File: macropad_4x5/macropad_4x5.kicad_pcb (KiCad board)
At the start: 2 copper layers, 76.2 x 95.2 mm, 41 parts

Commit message: Updated schematic and pcb routing
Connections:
- B1 pad 17: col0 -> col2
- B1 pad 18: col1 -> col3
- B1 pad 19: col2 -> col1
- B1 pad 20: col3 -> col0
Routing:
- net row3: track 0.00 -> 140.5 mm
- net row4: track 0.00 -> 140.5 mm
- net col0: track 0.00 -> 131.3 mm
- net col3: track 0.00 -> 130.1 mm
- net row2: track 0.00 -> 122.9 mm
- net row0: track 0.00 -> 98.4 mm
- net col1: track 0.00 -> 96.6 mm
- net row1: track 0.00 -> 91.9 mm
- net col2: track 0.00 -> 88.6 mm
- net Net-(D4-Pad2): track 0.00 -> 23.3 mm
- net Net-(D8-Pad2): track 0.00 -> 23.3 mm
- net Net-(D16-Pad2): track 0.00 -> 23.3 mm
- net Net-(D5-Pad2): track 0.00 -> 23.3 mm
- net Net-(D3-Pad2): track 0.00 -> 23.3 mm
- net Net-(D12-Pad2): track 0.00 -> 23.3 mm
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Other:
- net class Default: trace_width 0.25 -> 0.254

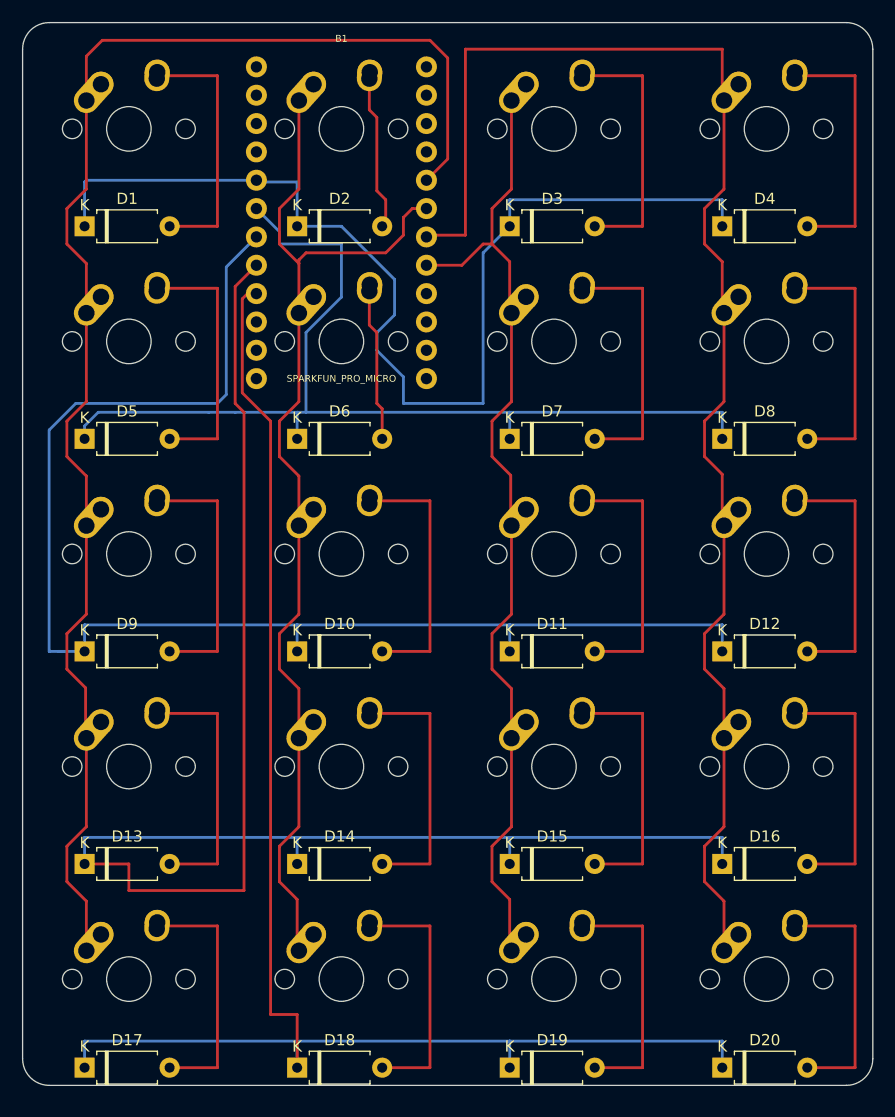
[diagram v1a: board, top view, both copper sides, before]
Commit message: Updated schematics and pcb design to clean it up
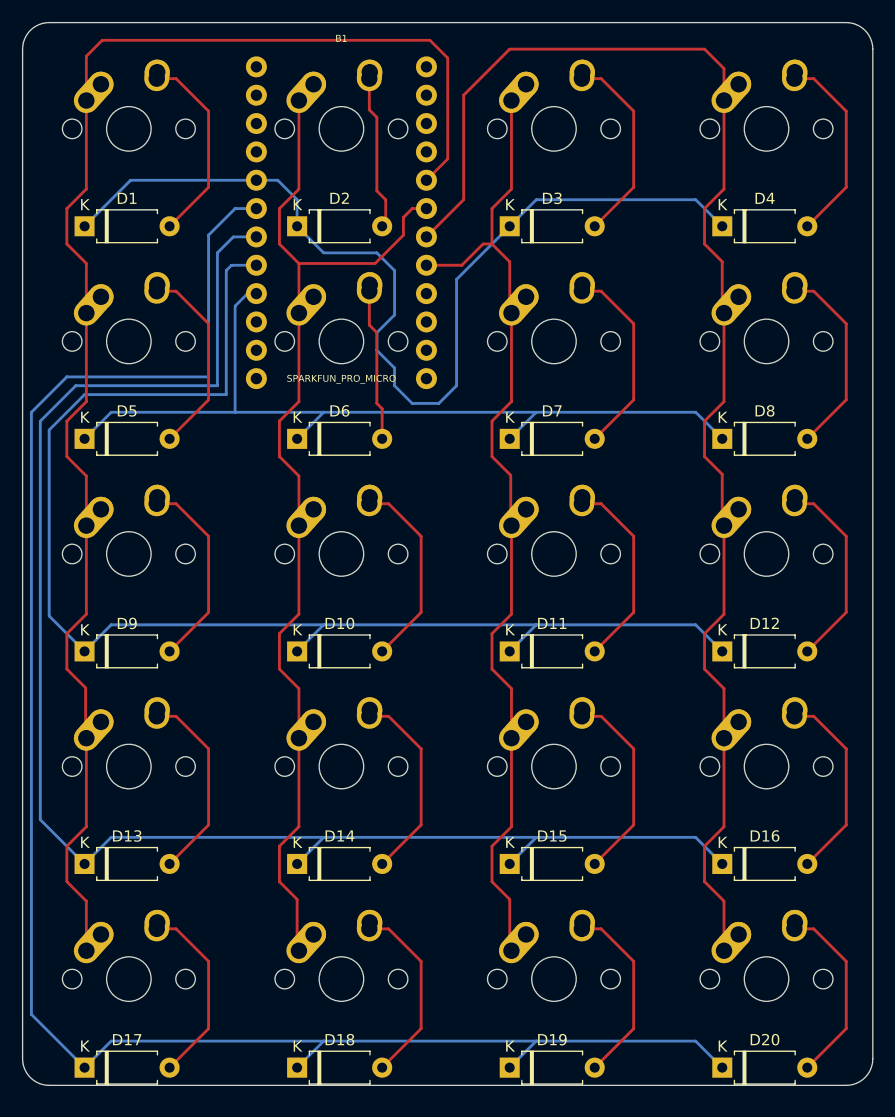
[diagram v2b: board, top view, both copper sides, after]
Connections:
- B1 pad 6: row1 -> row4
- B1 pad 7: row2 -> row3
- B1 pad 8: row3 -> row2
- B1 pad 9: row4 -> row1
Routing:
- net row4: track 140.5 -> 164.9 mm
- net row1: track 91.9 -> 78.5 mm
- net row0: track 98.4 -> 90.3 mm
- net Net-(D4-Pad2): track 23.3 -> 18.0 mm
- net Net-(D8-Pad2): track 23.3 -> 18.0 mm
- net Net-(D12-Pad2): track 23.3 -> 18.0 mm
- net Net-(D17-Pad2): track 22.5 -> 17.2 mm
- net Net-(D18-Pad2): track 22.5 -> 17.2 mm
- net Net-(D5-Pad2): track 23.3 -> 18.0 mm
- net Net-(D19-Pad2): track 22.5 -> 17.2 mm
- net Net-(D15-Pad2): track 23.3 -> 18.0 mm
- net Net-(D7-Pad2): track 23.3 -> 18.0 mm
- net Net-(D3-Pad2): track 23.3 -> 18.0 mm
- net Net-(D20-Pad2): track 22.5 -> 17.3 mm
- net Net-(D13-Pad2): track 23.3 -> 18.1 mm
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
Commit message: Updated PCB
The pro micro was facing the wrong way previously. Also added more text
to the silk layers to help marking for use.
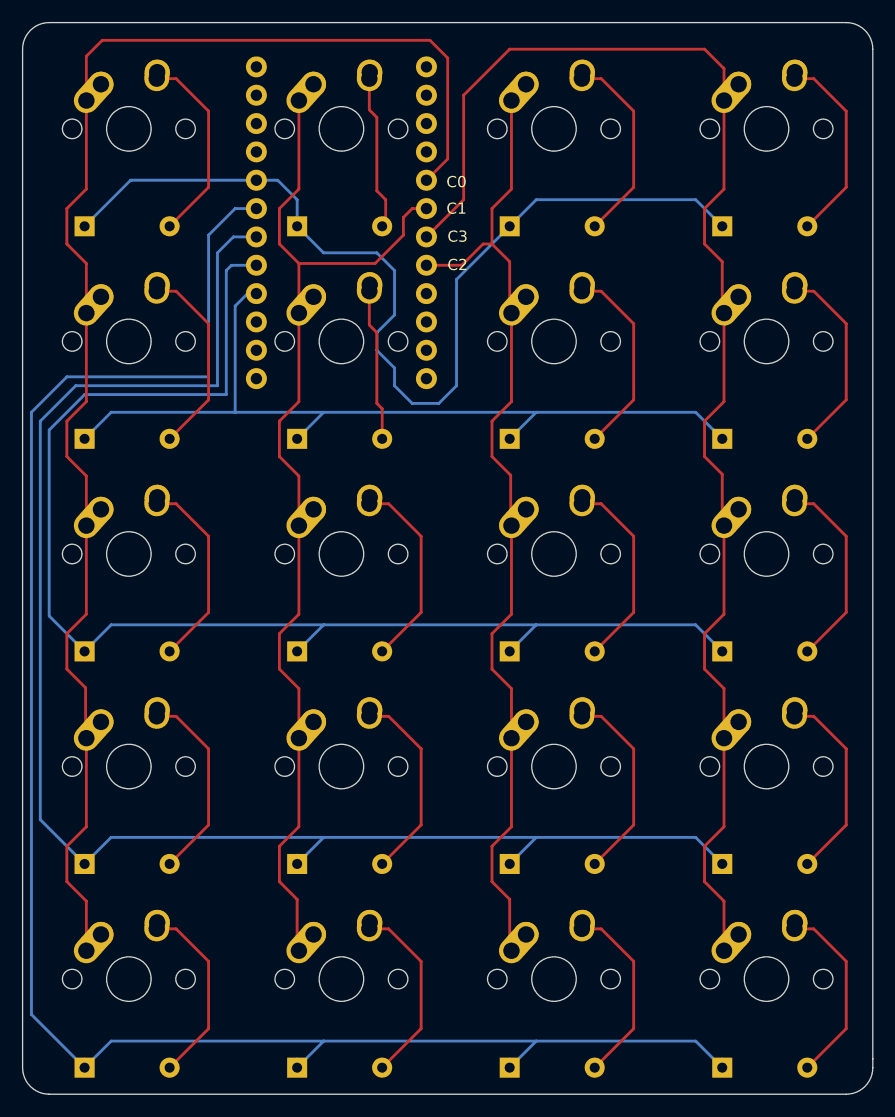
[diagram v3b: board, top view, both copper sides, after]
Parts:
- B1, D1, D10, D11, D12, D13, D14, D15, D16, D17, D18, D19, D2, D20, D3, D4, D5, D6, D7, D8, D9: moved to B.Cu
- turned B1 to 180 degrees
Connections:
- net Net-(B1-Pad1) renamed TXO
- net Net-(B1-Pad24) renamed RAW
- B1 pad 16: Net-(B1-Pad16) -> row1
- B1 pad 17: col2 -> row2
- B1 pad 18: col3 -> row3
- B1 pad 19: col1 -> row4
- B1 pad 20: col0 -> row0
- B1 pad 5: row0 -> col0
- B1 pad 6: row4 -> col1
- B1 pad 7: row3 -> col3
- B1 pad 8: row2 -> col2
- B1 pad 9: row1 -> Net-(B1-Pad9)
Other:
- board size 76.2 x 95.2 mm -> 76.2 x 96 mm
- board text added: "C0"
- board text added: "C1"
- board text added: "C2"
- board text added: "C3"
- board text added: "R0"
- board text added: "R1"
- board text added: "R2"
- board text added: "R3"
- board text added: "R4"
- board text added: "RAW"
- board text added: "TXO"

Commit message: Updated files for some comments
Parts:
- added REF**: MountingHole_2.2mm_M2_Pad_Via, MountingHole:MountingHole_2.2mm_M2_Pad_Via, F.Cu at (57.1, 101.6)
- added REF**: MountingHole_2.2mm_M2_Pad_Via, MountingHole:MountingHole_2.2mm_M2_Pad_Via, F.Cu at (95.2, 101.6)
- added REF**: MountingHole_2.2mm_M2_Pad_Via, MountingHole:MountingHole_2.2mm_M2_Pad_Via, F.Cu at (95.2, 42.9)
